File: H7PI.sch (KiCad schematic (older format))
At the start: 49 parts, among them J1 XKTF-015-N, J2 Header_2x10, J3 microUSB, J4 AFC07-S24ECA-00, J5 Header_2x20, J6 microUSB, J7 Header_1x2, J8 Header_1x1, J9 Header_1x1, Q1 CJ2101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

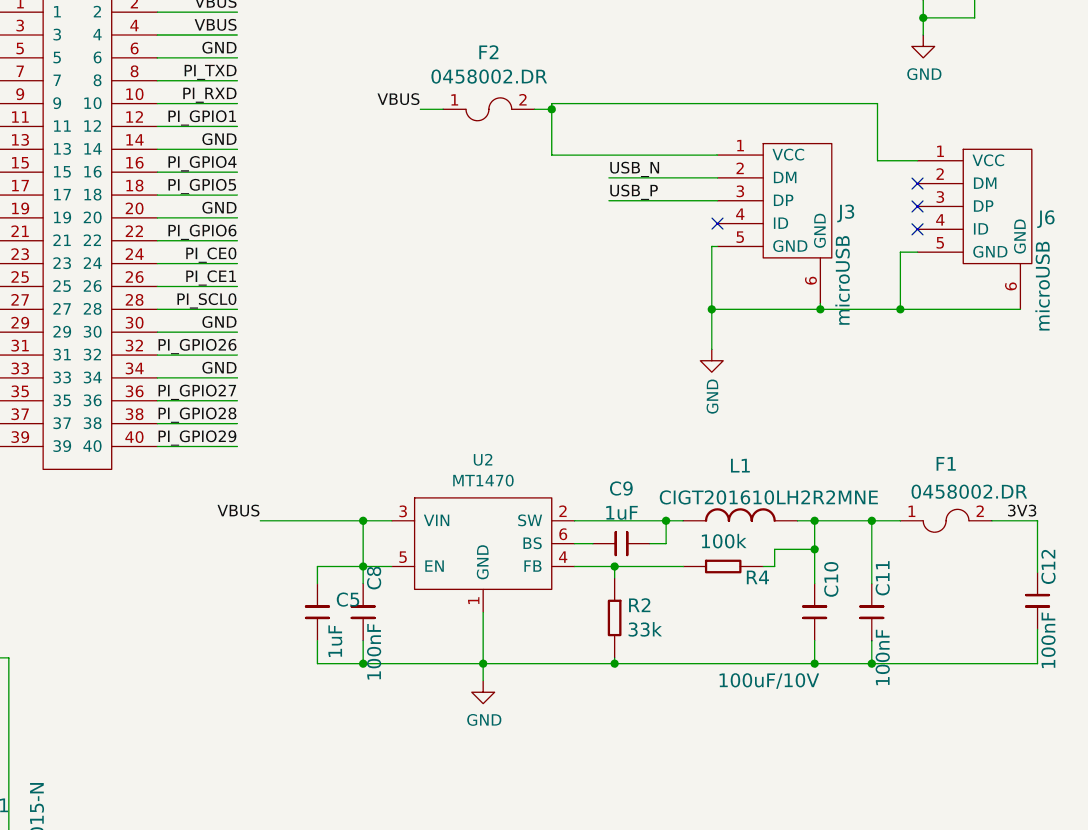
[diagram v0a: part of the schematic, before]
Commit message: v0.3 1. 增加电压支持到12V 2. 增加双USB口通信（不能同时用） 3. 增加USB通孔，用于底板扩展，正常为DNP状态
Signed-off-by: fuhua-chen <fuhua-chen@outlook.com>
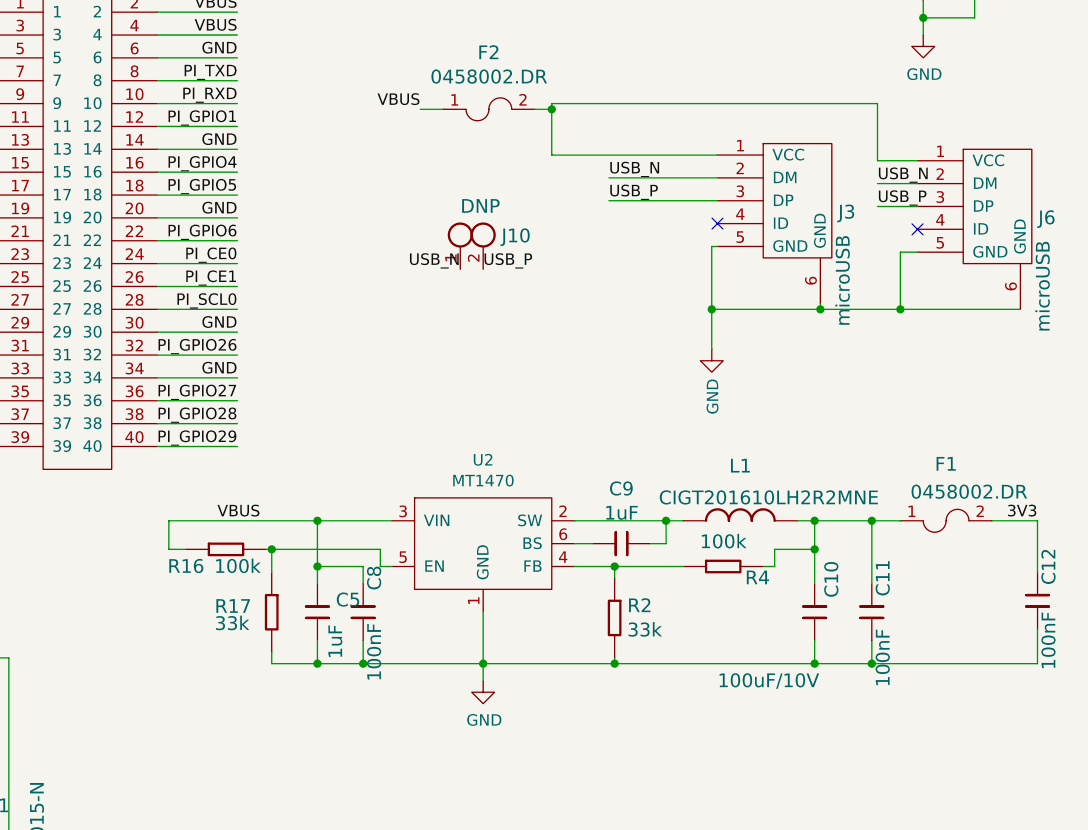
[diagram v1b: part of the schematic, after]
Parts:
- added J10: DNP, PinHeader_1x02_P2.54mm_Vertical, symbol connector:Header_1x2
- added R16: 100k, R_0402_1005Metric, symbol resistor:0402WGF1003TCE
- added R17: 33k, R_0402_1005Metric, symbol resistor:0402WGF3302TCE
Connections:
- net GND: now also R17.2
- net USB_N: now also J6.2 (DM), J10.1
- net USB_P: now also J6.3 (DP), J10.2
- net VBUS: now also R16.1; no longer U2.5 (EN)
- new net: R16.2, R17.1, U2.5 (EN)
- no-connect marks 8 -> 6
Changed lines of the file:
@@
 Sheet 1 1
 Title "H7PI"
-Date "2019-11-23"
-Rev "0.1"
+Date "2019-12-28"
+Rev "0.3"
 Comp "HTCTEK"
 Comment1 "fuhua-chen"
@@
 	1    0    0    -1
 $EndComp
-Text Label 9200 4200 0    50   ~ 0
+Text Label 8550 4600 2    50   ~ 0
 USB_N
-Text Label 9200 4300 0    50   ~ 0
+Text Label 8650 4600 0    50   ~ 0
 USB_P
 $Comp
@@
 Text Label 7675 5700 2    50   ~ 0
 VBUS
-Wire Wire Line
-	8250 5700 8125 5700
-Wire Wire Line
-	8250 5900 8125 5900
-Wire Wire Line
-	8125 5900 8125 5700
-Connection ~ 8125 5700
 $Comp
 L capacitor:0402B104K500NT C8
@@
 Wire Wire Line
 	8125 5975 8125 5900
-Connection ~ 8125 5900
 Wire Wire Line
 	8125 6225 8125 6325
@@
 	10350 6325 10350 6225
 Connection ~ 10100 6325
-Wire Wire Line
-	7675 5700 8125 5700
 Text Label 11075 5700 2    50   ~ 0
 3V3
@@
 Wire Wire Line
 	2125 6375 1775 6375
-NoConn ~ 10550 4225
-NoConn ~ 10550 4325
 NoConn ~ 10550 4425
 NoConn ~ 9675 4400
@@
 	9050 5700 9450 5700
 Connection ~ 9450 5700
+Wire Wire Line
+	7925 5900 7925 5700
+Connection ~ 7925 5900
+Connection ~ 7925 5700
+Wire Wire Line
+	7925 5700 8250 5700
+Wire Wire Line
+	8250 5900 8200 5900
+Wire Wire Line
+	8200 5900 8200 5825
+Wire Wire Line
+	8200 5825 7725 5825
+Wire Wire Line
+	7275 5700 7275 5825
+Wire Wire Line
+	7275 5825 7350 5825
+Wire Wire Line
+	7275 5700 7925 5700
+Wire Wire Line
+	7725 6275 7725 6325
+Wire Wire Line
+	7725 6325 7925 6325
+Connection ~ 7925 6325
+Wire Wire Line
+	7725 5925 7725 5825
+Connection ~ 7725 5825
+Wire Wire Line
+	7725 5825 7700 5825
+$Comp
+L resistor:0402WGF1003TCE R16
+U 1 1 5E1CA2BF
+P 7500 5825
+F 0 "R16" H 7350 5750 60  0000 C CNN
+F 1 "100k" H 7575 5750 60  0000 C CNN
+F 2 "R_0402_1005Metric" H 8500 6125 60  0001 C CNN
+F 3 "" H 7750 6475 60  0001 C CNN
+F 4 "UniOhm" H 7500 6025 50  0001 C CNN "Manufacturer"
+F 5 "0402WGF1003TCE" H 7600 6125 50  0001 C CNN "PartNumber"
+F 6 "https://item.szlcsc.com/26484.html" H 7700 6225 50  0001 C CNN "Supplier"
+F 7 "C25741" H 7150 6325 50  0001 C CNN "Sku"
+	1    7500 5825
+	1    0    0    -1
+$EndComp
+$Comp
+L resistor:0402WGF3302TCE R17
+U 1 1 5E1CAC33
+P 7725 6075
+F 0 "R17" V 7725 5825 60  0000 L CNN
+F 1 "33k" V 7800 5825 60  0000 L CNN
+F 2 "R_0402_1005Metric" H 8725 6375 60  0001 C CNN
+F 3 "https://atta.szlcsc.com/upload/public/pdf/source/20170920/C25778_1505901538742983352.pdf" H 7975 6725 60  0001 C CNN
+F 4 "UniOhm" H 7725 6275 50  0001 C CNN "Manufacturer"
+F 5 "0402WGF3302TCE" H 7825 6375 50  0001 C CNN "PartNumber"
+F 6 "https://item.szlcsc.com/26522.html" H 7925 6475 50  0001 C CNN "Supplier"
+F 7 "C25779" H 7375 6575 50  0001 C CNN "Sku"
+	1    7725 6075
+	0    1    1    0
+$EndComp
+$Comp
+L connector:Header_1x2 J10
+U 1 1 5E1ECC8C
+P 8550 4450
+F 0 "J10" H 8730 4446 60  0000 L CNN
+F 1 "DNP" H 8550 4575 60  0000 L CNN
+F 2 "PinHeader_1x02_P2.54mm_Vertical" H 8450 4550 60  0001 C CNN
+F 3 "" H 8550 4450 60  0001 C CNN
+	1    8550 4450
+	1    0    0    -1
+$EndComp
+Text Label 9200 4200 0    50   ~ 0
+USB_N
+Text Label 9200 4300 0    50   ~ 0
+USB_P
+Text Label 10375 4225 0    50   ~ 0
+USB_N
+Text Label 10375 4325 0    50   ~ 0
+USB_P
+Wire Wire Line
+	10550 4325 10375 4325
+Wire Wire Line
+	10375 4225 10550 4225
 $EndSCHEMATC
